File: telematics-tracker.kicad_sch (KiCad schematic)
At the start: 0 parts

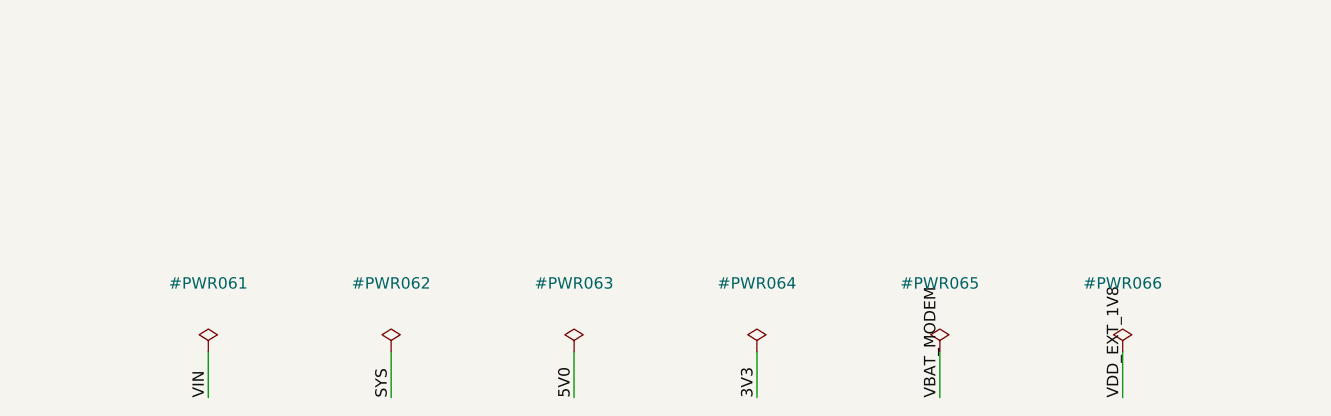
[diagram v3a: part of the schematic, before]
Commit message: M2: F-8 in-stock sweep complete - all TBD-F8 parts selected and wired
Selections (all datasheet- or API-verified, see design-log):
  Q1/Q2  AM2390N-TP 150V 4A SOT-23   C51886143 (F-10: gate drive caveat)
  D3     Nexperia PESD1CAN,215       C15771 (single dual-line part
         replaces the D3/D4 placeholder pair)
  L2     TDK ACT45B-510-2P-TL003     C76584 (windings 1->4 / 2->3 per TDK
         circuit diagram; alt clone C48928226 in Alternate field)
  J1     XUNPU WAFER-MX3.0-12PZZ     C7588012 (Molex 43045 stock footprint)
  D5/6/10/11 BAV99 Nexperia          C2500
  D7/D8  SS310 MDD                   C15874 (F-11: SS3200 C65001 recommended)
  R11/12 60.4R 1% YAGEO              C228935
  DI 12k 1206                        C17912
  47k / 100k / 9.1k / 1M 0805        C17713 / C17407 / C17855 / C17514
  C22    4.7nF X7R Samsung           C1621
D2 upgraded to Littelfuse SMDJ100A   C1977839 (per U5 approval condition b)

Generator: third silent-merge failure mode found and guarded -
a label point landing mid-span on another net's wire segment. The guard
caught D3's CANL label sitting on L2's CANH stub (KiCad had reported it
only as a multiple_net_names warning). CAN pair verified by netlist:
CANH = J1.4+D3.1+L2.1, CANH_T = L2.4+R11+U4.7, same for CANL via 2->3.

ERC 0 errors.

Co-Authored-By: Claude Fable 5 <noreply@anthropic.com>
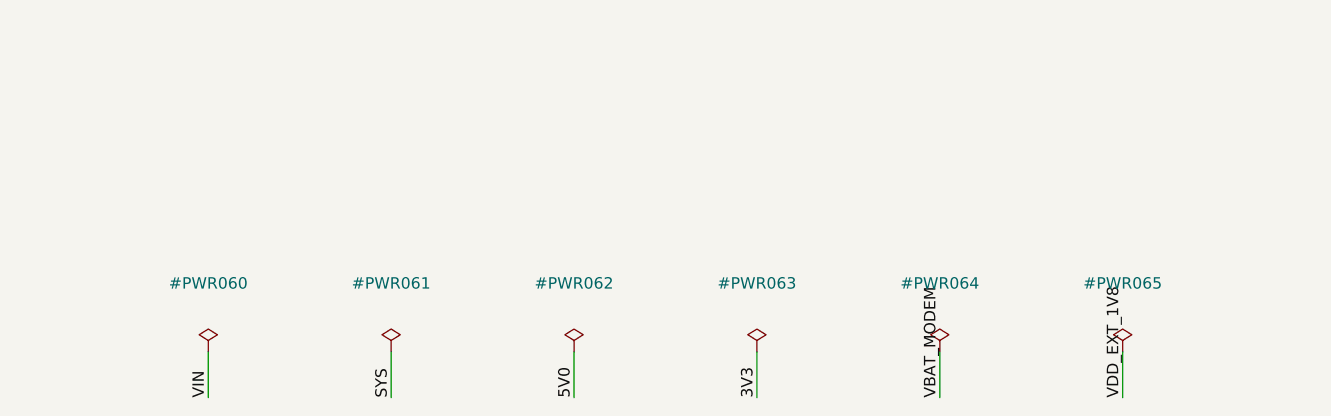
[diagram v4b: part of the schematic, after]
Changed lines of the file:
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@@
+		(dnp no)
+		(fields_autoplaced yes)
+		(property "Reference" "#PWR060"
+			(at 25.4 261.62 0)
+			(effects
+				(font
+					(size 1.27 1.27)
+				)
+			)
+		)
+		(property "Value" "PWR_FLAG"
+			(at 25.4 269.24 0)
+			(hide yes)
+			(effects
+				(font
+					(size 1.27 1.27)
+				)
+			)
+		)
+		(pin "1"
+		)
+		(instances
+			(project "telematics-tracker"
+				(path "/784bc421-9fc7-43cb-bfc3-562714cb3f68"
+					(reference "#PWR060")
+					(unit 1)
+				)
+			)
+		)
+	)
+	(symbol
+		(lib_id "power:PWR_FLAG")
+		(at 45.72 269.24 0)
+		(unit 1)
+		(exclude_from_sim no)
+		(in_bom yes)
+		(on_board yes)
 		(dnp no)
 		(fields_autoplaced yes)
 		(property "Reference" "#PWR061"
-			(at 25.4 261.62 0)
-			(effects
-				(font
-					(size 1.27 1.27)
-				)
-			)
-		)
-		(property "Value" "PWR_FLAG"
-			(at 25.4 269.24 0)
+			(at 45.72 261.62 0)
+			(effects
+				(font
+					(size 1.27 1.27)
+				)
+			)
+		)
+		(property "Value" "PWR_FLAG"
+			(at 45.72 269.24 0)
 			(hide yes)
 			(effects
@@
 	(symbol
 		(lib_id "power:PWR_FLAG")
-		(at 45.72 269.24 0)
+		(at 66.04 269.24 0)
 		(unit 1)
 		(exclude_from_sim no)
@@
 		(fields_autoplaced yes)
 		(property "Reference" "#PWR062"
-			(at 45.72 261.62 0)
-			(effects
-				(font
-					(size 1.27 1.27)
-				)
-			)
-		)
-		(property "Value" "PWR_FLAG"
-			(at 45.72 269.24 0)
+			(at 66.04 261.62 0)
+			(effects
+				(font
+					(size 1.27 1.27)
+				)
+			)
+		)
+		(property "Value" "PWR_FLAG"
+			(at 66.04 269.24 0)
 			(hide yes)
 			(effects
@@
 	(symbol
 		(lib_id "power:PWR_FLAG")
-		(at 66.04 269.24 0)
+		(at 86.36 269.24 0)
 		(unit 1)
 		(exclude_from_sim no)
@@
 		(fields_autoplaced yes)
 		(property "Reference" "#PWR063"
-			(at 66.04 261.62 0)
-			(effects
-				(font
-					(size 1.27 1.27)
-				)
-			)
-		)
-		(property "Value" "PWR_FLAG"
-			(at 66.04 269.24 0)
+			(at 86.36 261.62 0)
+			(effects
+				(font
+					(size 1.27 1.27)
+				)
+			)
+		)
+		(property "Value" "PWR_FLAG"
+			(at 86.36 269.24 0)
 			(hide yes)
 			(effects
@@
 	(symbol
 		(lib_id "power:PWR_FLAG")
-		(at 86.36 269.24 0)
+		(at 106.68 269.24 0)
 		(unit 1)
 		(exclude_from_sim no)
@@
 		(fields_autoplaced yes)
 		(property "Reference" "#PWR064"
-			(at 86.36 261.62 0)
-			(effects
-				(font
-					(size 1.27 1.27)
-				)
-			)
-		)
-		(property "Value" "PWR_FLAG"
-			(at 86.36 269.24 0)
+			(at 106.68 261.62 0)
+			(effects
+				(font
+					(size 1.27 1.27)
+				)
+			)
+		)
+		(property "Value" "PWR_FLAG"
+			(at 106.68 269.24 0)
 			(hide yes)
 			(effects
@@
 	(symbol
 		(lib_id "power:PWR_FLAG")
-		(at 106.68 269.24 0)
+		(at 127 269.24 0)
 		(unit 1)
 		(exclude_from_sim no)
@@
 		(fields_autoplaced yes)
 		(property "Reference" "#PWR065"
-			(at 106.68 261.62 0)
-			(effects
-				(font
-					(size 1.27 1.27)
-				)
-			)
-		)
-		(property "Value" "PWR_FLAG"
-			(at 106.68 269.24 0)
+			(at 127 261.62 0)
+			(effects
+				(font
+					(size 1.27 1.27)
+				)
+			)
+		)
+		(property "Value" "PWR_FLAG"
+			(at 127 269.24 0)
 			(hide yes)
 			(effects
@@
 					(unit 1)
 				)
-			)
-		)
-	)
-	(symbol
-		(lib_id "power:PWR_FLAG")
-		(at 127 269.24 0)
-		(unit 1)
-		(exclude_from_sim no)
-		(in_bom yes)
-		(on_board yes)
-		(dnp no)
-		(fields_autoplaced yes)
-		(property "Reference" "#PWR066"
-			(at 127 261.62 0)
-			(effects
-				(font
-					(size 1.27 1.27)
-				)
-			)
-		)
-		(property "Value" "PWR_FLAG"
-			(at 127 269.24 0)
-			(hide yes)
-			(effects
-				(font
-					(size 1.27 1.27)
-				)
-			)
-		)
-		(pin "1"
-		)
-		(instances
-			(project "telematics-tracker"
-				(path "/784bc421-9fc7-43cb-bfc3-562714cb3f68"
-					(reference "#PWR066")
-					(unit 1)
-				)
